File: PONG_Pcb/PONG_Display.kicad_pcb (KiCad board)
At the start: 2 copper layers, 95.2 x 66.4 mm, 72 parts, among them J1 LED_Display_Conn, J2 Input_Supply+5V, J3 DHT22_Conn, J4 LightSensor_Conn, J5 PIR_Sensor_Conn, J6 AVR-ISP-6, J7 Conn_01x04, J8 ESP_Conn, J9 ESP_Prog_Conn, Q1 BSS138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

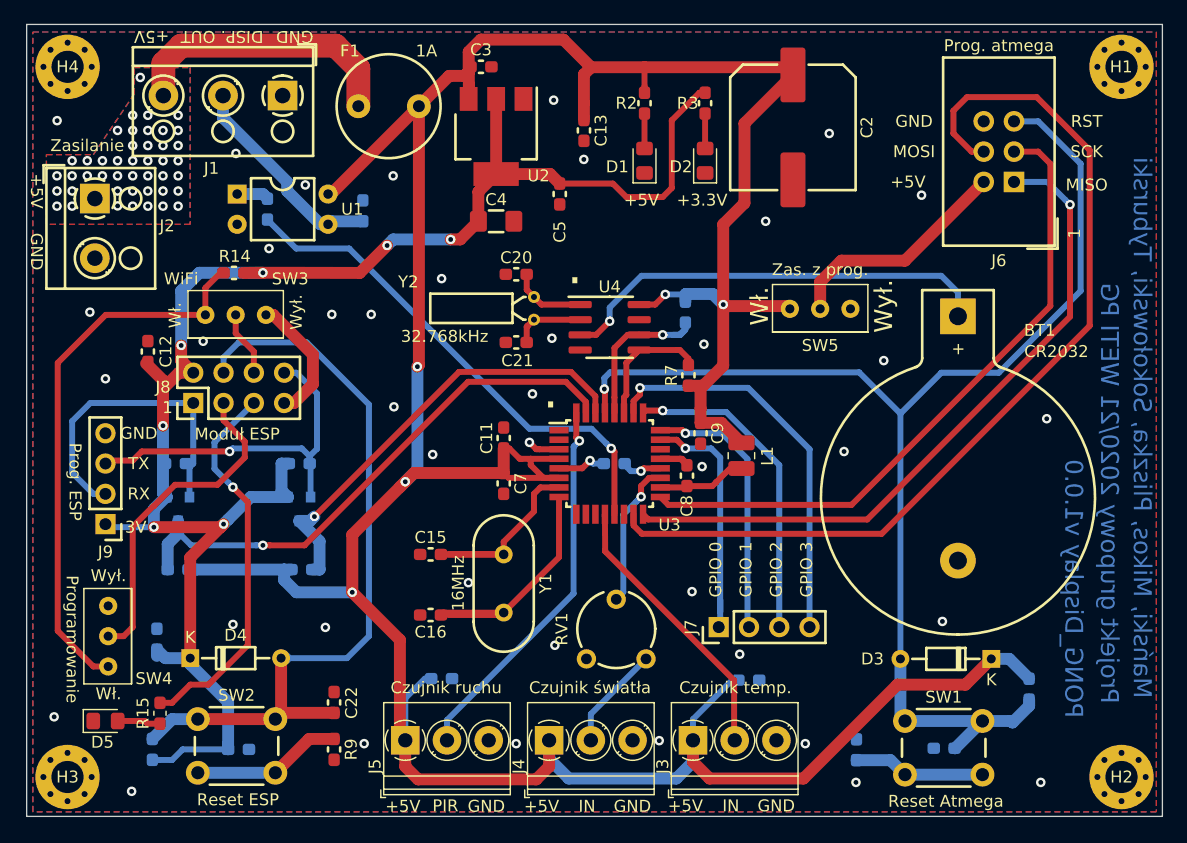
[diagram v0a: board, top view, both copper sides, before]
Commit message: Poprawki layoutu
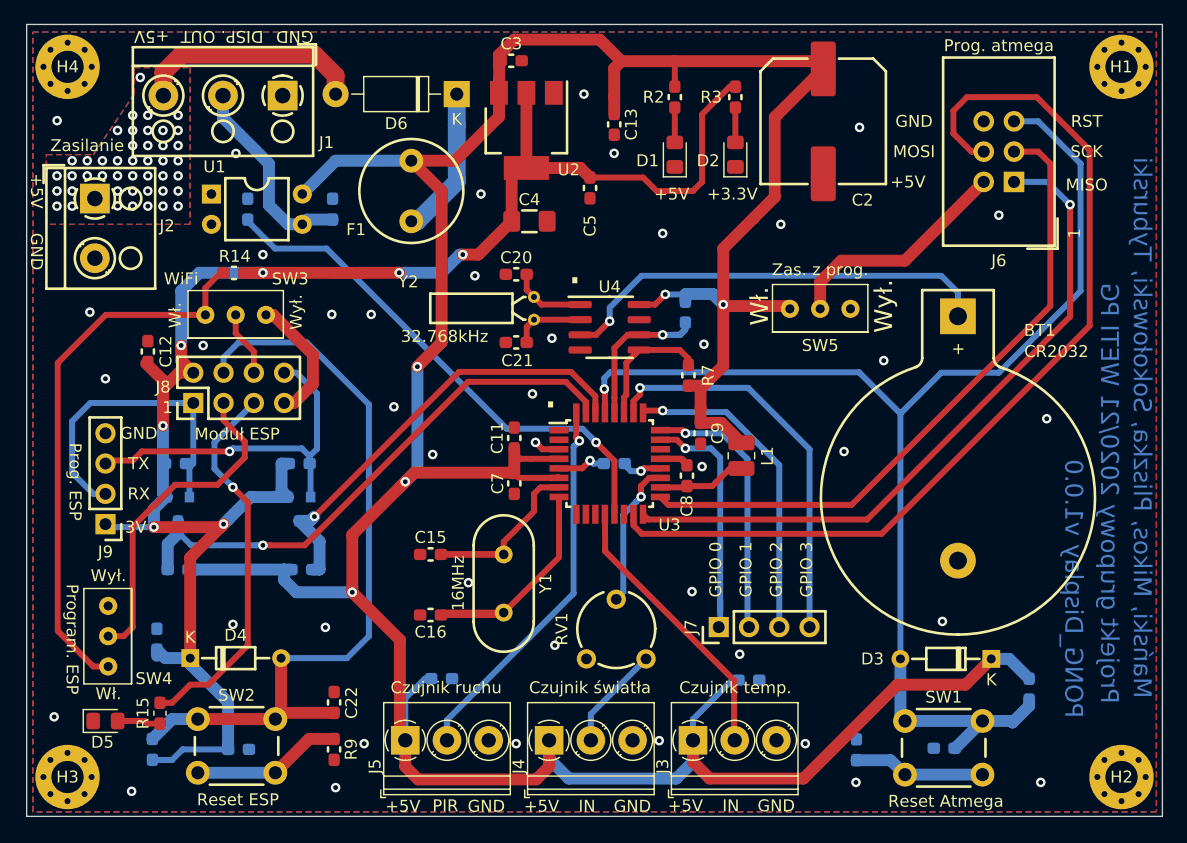
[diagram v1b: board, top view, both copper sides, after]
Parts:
- removed C1: 100n, Capacitor_SMD:C_0603_1608Metric_Pad1.05x0.95mm_HandSolder
- added D6: 1N4001, Diode_THT:D_DO-41_SOD81_P10.16mm_Horizontal, F.Cu at (48.8, 17.3)
- added R16: 470R, Resistor_SMD:R_0603_1608Metric_Pad1.05x0.95mm_HandSolder, B.Cu at (38.4, 26.9)
- moved F1 4.62 mm to (45.0, 22.9), turned to 270 degrees
- moved C4 2.79 mm to (54.9, 27.9)
- moved C3 2.59 mm to (53.3, 14.5)
- moved C13 2.59 mm to (62.0, 19.8)
- moved C5 2.59 mm to (59.9, 25.1)
- moved U2 2.59 mm to (54.6, 20.3)
- moved C2 2.59 mm to (79.5, 19.6)
- moved D1 2.59 mm to (67.1, 22.4)
- moved D2 2.59 mm to (72.1, 22.4)
- moved R2 2.59 mm to (67.1, 17.5)
- moved R3 2.59 mm to (72.1, 17.5)
- moved U1 2.16 mm to (28.2, 25.7)
- moved R1 1.65 mm to (31.2, 26.9)
- moved C11 0.89 mm to (53.6, 46.1)
- moved C7 0.89 mm to (53.6, 49.9)
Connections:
- F1 pad 2: +5VA -> Net-(D6-Pad1)
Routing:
- net Net-(D6-Pad1): track 0.00 -> 12.5 mm
- net +5VA: track 23.7 -> 19.3 mm
- net +3V3: track 143.4 -> 147.0 mm
- net Net-(R1-Pad1): track 2.52 -> 0.00 mm
- net /MikrokontrolerAtmega/LED_DATA: track 42.6 -> 43.8 mm
- net /Wyswietlacz LED/LED_DATA_ISO: track 17.6 -> 17.0 mm
- net +5V: track 287.5 -> 287.0 mm
- net GND: track 22.7 -> 22.2 mm, vias 42 -> 43
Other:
- board text added: "Program. ESP"
- board text removed: "1A"
- board text removed: "Programowanie"

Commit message: Drobne poprawki
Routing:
- net Net-(R1-Pad1): track 0.00 -> 3.21 mm
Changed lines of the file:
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@@
     (thickness 1.6)
     (drawings 65)
-    (tracks 587)
+    (tracks 589)
     (zones 0)
     (modules 73)
@@
   )
   (setup
-    (last_trace_width 1)
+    (last_trace_width 0.5)
     (user_trace_width 0.3)
     (user_trace_width 0.5)
@@
   (via (at 72.5 64.25) (size 0.8) (drill 0.4) (layers F.Cu B.Cu) (net 1))
   (via (at 68.5 59) (size 0.8) (drill 0.4) (layers F.Cu B.Cu) (net 1))
-  (via (at 57 63.5) (size 0.8) (drill 0.4) (layers F.Cu B.Cu) (net 1))
+  (via (at 56.642 64.77) (size 0.8) (drill 0.4) (layers F.Cu B.Cu) (net 1))
   (via (at 49.75 58.25) (size 0.8) (drill 0.4) (layers F.Cu B.Cu) (net 1))
   (via (at 41 71.75) (size 0.8) (drill 0.4) (layers F.Cu B.Cu) (net 1))
@@
   (segment (start 61.594988 35.179012) (end 61.594988 36.322) (width 0.5) (layer B.Cu) (net 2))
   (segment (start 90.805 33.91) (end 89.407 32.512) (width 0.5) (layer B.Cu) (net 2))
-  (segment (start 36.209 27.799) (end 35.814 28.194) (width 1) (layer B.Cu) (net 3))
-  (segment (start 38.354 27.799) (end 36.209 27.799) (width 1) (layer B.Cu) (net 3))
   (segment (start 33.02 26.596484) (end 34.617516 28.194) (width 1) (layer B.Cu) (net 3))
   (segment (start 33.02 23.114) (end 33.02 26.596484) (width 1) (layer B.Cu) (net 3))
@@
   (segment (start 29.163 17.399) (end 29.163 19.257) (width 1) (layer B.Cu) (net 3))
   (segment (start 29.163 19.257) (end 33.02 23.114) (width 1) (layer B.Cu) (net 3))
+  (segment (start 37.959 28.194) (end 35.814 28.194) (width 1) (layer B.Cu) (net 3))
+  (segment (start 38.354 27.799) (end 37.959 28.194) (width 1) (layer B.Cu) (net 3))
   (segment (start 67.945 34.0725) (end 66.8925 34.0725) (width 0.3) (layer B.Cu) (net 4))
   (via (at 66.2575 34.0725) (size 0.8) (drill 0.4) (layers F.Cu B.Cu) (net 4))
@@
   (segment (start 30.226 35.79) (end 30.226 37.338) (width 0.5) (layer F.Cu) (net 28) (status 10))
   (segment (start 31.75 38.862) (end 31.75 40.64) (width 0.5) (layer F.Cu) (net 28) (status 20))
+  (segment (start 30.847 25.654) (end 31.242 26.049) (width 0.5) (layer B.Cu) (net 29))
+  (segment (start 28.194 25.654) (end 30.847 25.654) (width 0.5) (layer B.Cu) (net 29))
   (via (at 60.452 46.482) (size 0.8) (drill 0.4) (layers F.Cu B.Cu) (net 30))
   (segment (start 61.995 52.51) (end 61.995 48.025) (width 0.5) (layer F.Cu) (net 30) (status 10))

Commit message: Poprawki
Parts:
- added C1: 100n, Capacitor_SMD:C_0603_1608Metric_Pad1.05x0.95mm_HandSolder, F.Cu at (39.6, 29.0)
- moved R16 5.08 mm to (33.3, 26.9)
- moved R1 0.76 mm to (30.5, 26.9)
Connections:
- R16 pad 1: /Wyswietlacz LED/LED_DATA_ISO -> Net-(C1-Pad1)
- R16 pad 2: GND -> /Wyswietlacz LED/LED_DATA_ISO
- U1 pad 3: /Wyswietlacz LED/LED_DATA_ISO -> Net-(C1-Pad1)
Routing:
- net /Wyswietlacz LED/LED_DATA_ISO: track 17.0 -> 10.4 mm
- net Net-(C1-Pad1): track 0.00 -> 6.56 mm
- net Net-(R1-Pad1): track 3.21 -> 2.45 mm
- net /MikrokontrolerAtmega/LED_DATA: track 43.8 -> 44.4 mm
- net GND: vias 43 -> 45
